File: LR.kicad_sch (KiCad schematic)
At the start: 41 parts, among them J7 Conn_01x01_Pin, J8 Conn_01x01_Pin, J9 Conn_01x01_Pin, Q13 NMOS, Q14 NMOS, Q15 NMOS, Q16 NMOS, Q17 NMOS, Q18 NMOS, U5 OPA2196xDGK, U6 MCT8329A1IREER

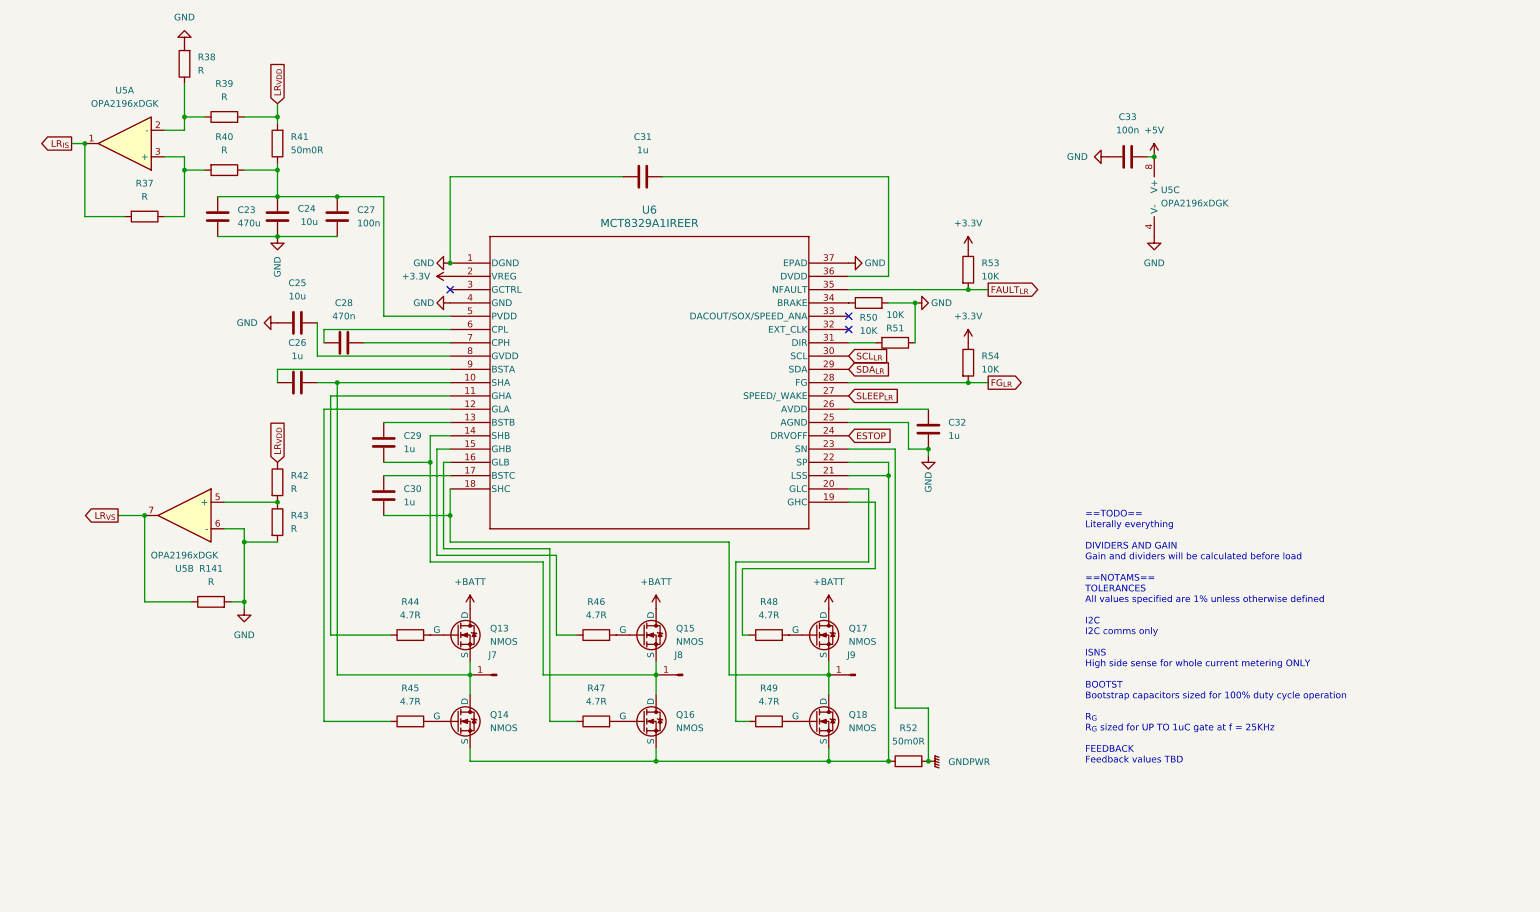
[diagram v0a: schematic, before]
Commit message: The great decluttering
Moved all possible controls to I2C, part selection commenced, IOs assigned pending comms schema
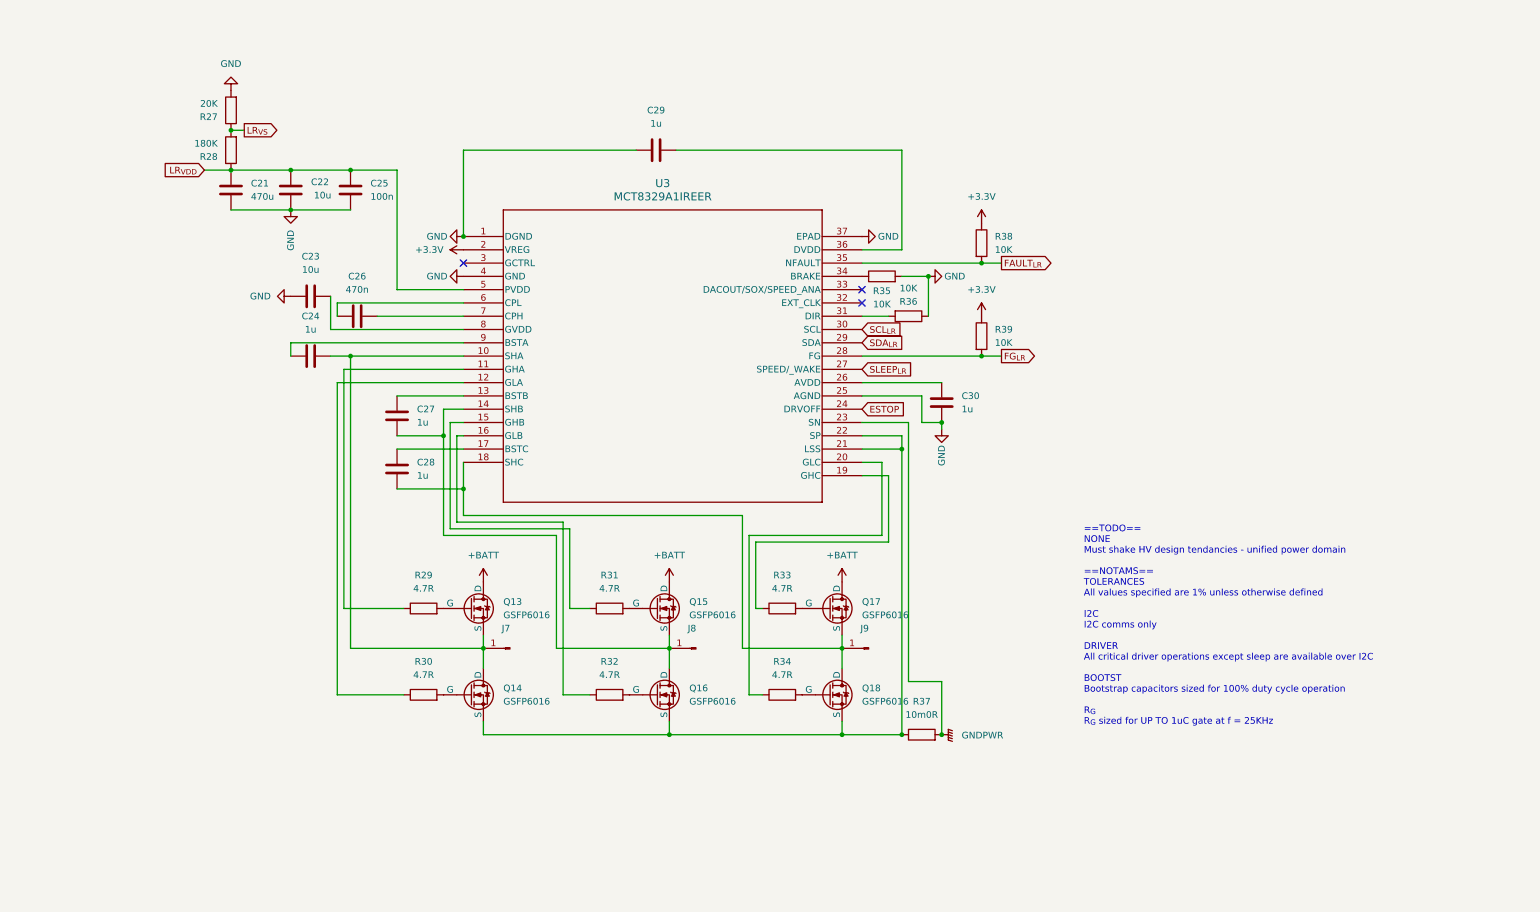
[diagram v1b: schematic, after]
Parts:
- removed C31, C32: 1u, Capacitor_SMD:C_0603_1608Metric, symbol Device:C
- removed C33: 100n, Capacitor_SMD:C_0603_1608Metric, symbol Device:C
- removed R141, R40, R42, R43: R, Resistor_SMD:R_0603_1608Metric_Pad0.98x0.95mm_HandSolder, symbol Device:R
- removed R41, R52: 50m0R, Resistor_SMD:R_1206_3216Metric, symbol Device:R
- removed R44, R45, R46, R47, R48, R49: 4.7R, Resistor_SMD:R_1206_3216Metric, symbol Device:R
- removed R50, R51, R53, R54: 10K, Resistor_SMD:R_0603_1608Metric_Pad0.98x0.95mm_HandSolder, symbol Device:R
- removed U5: OPA2196xDGK, Package_SO:VSSOP-8_3x3mm_P0.65mm, symbol Amplifier_Operational:OPA2196xDGK
- removed U6: MCT8329A1IREER, footprints:WQFN36_REE_TEX, symbol MCT8329:MCT8329A1IREER
- added C21: 470u, Capacitor_SMD:C_0603_1608Metric, symbol Device:C
- added C22: 10u, Capacitor_SMD:C_0603_1608Metric, symbol Device:C
- added R27: 20K, Resistor_SMD:R_0603_1608Metric_Pad0.98x0.95mm_HandSolder, symbol Device:R
- added R28: 180K, Resistor_SMD:R_0603_1608Metric_Pad0.98x0.95mm_HandSolder, symbol Device:R
- added R29, R30, R31, R32, R33, R34: 4.7R, Resistor_SMD:R_1206_3216Metric, symbol Device:R
- added R35, R36: 10K, Resistor_SMD:R_0603_1608Metric_Pad0.98x0.95mm_HandSolder, symbol Device:R
- added U3: MCT8329A1IREER, footprints:WQFN36_REE_TEX, symbol MCT8329:MCT8329A1IREER
- C23: value 470u -> 10u
- C24: value 10u -> 1u
- C25: value 10u -> 100n
- C26: value 1u -> 470n
- C27: value 100n -> 1u
- C28: value 470n -> 1u
- Q13, Q14, Q15, Q16, Q17, Q18: value NMOS -> GSFP6016; footprint (none) -> Package_DFN_QFN:PQFN-8-EP_6x5mm_P1.27mm_Generic
- R37: value R -> 10m0R; footprint Resistor_SMD:R_0603_1608Metric_Pad0.98x0.95mm_HandSolder -> Resistor_SMD:R_1206_3216Metric
- R38, R39: value R -> 10K
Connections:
- net LR_{IS} is gone; now on net GNDPWR: R37.2
- net +3.3V: now also R38.1, R39.1, U3.2 (VREG)
- net ESTOP: now also U3.24 (DRVOFF)
- net FAULT_{LR}: now also R38.2, U3.35 (NFAULT)
- net FG_{LR}: now also R39.2, U3.28 (FG)
- net GND: now also C23.1, C25.2, C29.1, C30.1, C21.2, C22.2, R27.2, R35.2, R36.1, U3.1 (DGND), U3.25 (AGND), U3.37 (EPAD), U3.4 (GND); no longer C23.2, C24.2, C25.1, C27.2, R38.2
- net GNDPWR: now also U3.23 (SN)
- net LR_{VDD}: now also C25.1, C21.1, C22.1, R28.1, U3.5 (PVDD); no longer R39.2
- net LR_{VS}: now also R27.1, R28.2
- net SCL_{LR}: now also U3.30 (SCL)
- net SDA_{LR}: now also U3.29 (SDA)
- net SLEEP_{LR}: now also U3.27 (SPEED/_WAKE)
- net at Q16.2 (G): now also R32.2
- net at J7.1 (Pin_1), Q13.3 (S), Q14.1 (D): now also C24.1, U3.10 (SHA); no longer C26.1
- net at Q14.2 (G): now also R30.2
- net at Q14.3 (S), Q16.3 (S), Q18.3 (S): now also R37.1, U3.21 (LSS), U3.22 (SP)
- net at Q13.2 (G): now also R29.2
- net at J9.1 (Pin_1), Q17.3 (S), Q18.1 (D): now also C28.2, U3.18 (SHC); no longer C30.2
- net at C26.2: now also U3.7 (CPH)
- net at Q18.2 (G): now also R34.2
- net at C28.1: now also U3.17 (BSTC)
- net at J8.1 (Pin_1), Q15.3 (S), Q16.1 (D): now also C27.2, U3.14 (SHB); no longer C29.2
- net at Q17.2 (G): now also R33.2
- net at Q15.2 (G): now also R31.2
- new net: R33.1, U3.19 (GHC)
- new net: C30.2, U3.26 (AVDD)
- new net: C29.2, U3.36 (DVDD)
- new net: C27.1, U3.13 (BSTB)
- new net: R32.1, U3.16 (GLB)
- new net: R29.1, U3.11 (GHA)
- new net: R30.1, U3.12 (GLA)
- new net: R31.1, U3.15 (GHB)
- new net: R34.1, U3.20 (GLC)
- new net: R36.2, U3.31 (DIR)
- new net: R35.1, U3.34 (BRAKE)
- new net: C26.1, U3.6 (CPL)
- new net: C23.2, U3.8 (GVDD)
- new net: C24.2, U3.9 (BSTA)
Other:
- note added: "==TODO== NONE Must shake HV design tendancies - unified power domain ==NOTAMS== TOLERANCES All values specified are 1% unless otherwise defined I2C I2C comms only DRIVER All critical driver operations except sleep are available over I2C BOOTST Bootstrap capacitors sized for 100% duty cycle operation R_{G} R_{G} sized for UP TO 1uC gate at f = 25KHz"
- note removed: "==TODO== Literally everything DIVIDERS AND GAIN Gain and dividers will be calculated before load ==NOTAMS== TOLERANCES All values specified are 1% unless otherwise defined I2C I2C comms only ISNS High side sense for whole current metering ONLY BOOTST Bootstrap capacitors sized for 100% duty cycle operation R_{G} R_{G} sized for UP TO 1uC gate at f = 25KHz FEEDBACK Feedback values TBD"

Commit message: Powerstage
Powerstage layout, non critical changes to schematic
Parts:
- removed C25: 100n, Capacitor_SMD:C_0603_1608Metric, symbol Device:C
- removed J7, J8, J9: Conn_01x01_Pin, symbol Connector:Conn_01x01_Pin
- removed Q13, Q14, Q15, Q16, Q17, Q18: GSFP6016, Package_DFN_QFN:PQFN-8-EP_6x5mm_P1.27mm_Generic, symbol Simulation_SPICE:NMOS
- removed R37: 10m0R, Resistor_SMD:R_1206_3216Metric, symbol Device:R
- added J3: 1724470408, footprints:CONN08_1724470408_MOL, symbol 1724470408:1724470408
- added Q13, Q14, Q15, Q16, Q17, Q18: GSFP6016, Package_SO:PowerPAK_SO-8_Single, symbol Transistor_FET:SiR696DP
- added R37: WSL3637R0100FEA, WSL3637_VIS, symbol WSL3637R0100FEA:WSL3637R0100FEA
- C21: footprint Capacitor_SMD:C_0603_1608Metric -> Capacitor_THT:CP_Radial_D10.0mm_P5.00mm
- C22: footprint Capacitor_SMD:C_0603_1608Metric -> Capacitor_SMD:C_1210_3225Metric
- C23: footprint Capacitor_SMD:C_0603_1608Metric -> Capacitor_SMD:C_0402_1005Metric
- C24, C26, C27, C28, C29, C30: footprint Capacitor_SMD:C_0603_1608Metric -> Capacitor_SMD:C_0201_0603Metric
- R27, R28, R35, R36, R38, R39: footprint Resistor_SMD:R_0603_1608Metric_Pad0.98x0.95mm_HandSolder -> Resistor_SMD:R_0201_0603Metric
- R29, R30, R31, R32, R33, R34: value 4.7R -> 4R7; footprint Resistor_SMD:R_1206_3216Metric -> Resistor_SMD:R_0603_1608Metric
- U3: footprint footprints:WQFN36_REE_TEX -> WQFN36_REE_TEX
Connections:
- net GNDPWR: now also J3.4, J3.8, R37.4; no longer U3.23 (SN)
- net LR_{VDD}: now also Q13.5 (D), Q15.5 (D), Q17.5 (D)
- net at R29.2: now also Q13.4 (G)
- net at C24.1, U3.10 (SHA): now also J3.1, J3.5, Q13.1 (S), Q13.2 (S), Q13.3 (S), Q14.5 (D)
- net at C28.2, U3.18 (SHC): now also J3.3, J3.7, Q17.1 (S), Q17.2 (S), Q17.3 (S), Q18.5 (D)
- net at R34.2: now also Q18.4 (G)
- net at U3.21 (LSS), U3.22 (SP): now also R37.2
- net at R33.2: now also Q17.4 (G)
- net at R31.2: now also Q15.4 (G)
- net at C27.2, U3.14 (SHB): now also J3.2, J3.6, Q15.1 (S), Q15.2 (S), Q15.3 (S), Q16.5 (D)
- net at R32.2: now also Q16.4 (G)
- net at U3.6 (CPL): now also C26.2; no longer C26.1
- net at U3.7 (CPH): now also C26.1; no longer C26.2
- net at R30.2: now also Q14.4 (G)
- new net: Q14.1 (S), Q14.2 (S), Q14.3 (S), Q16.1 (S), Q16.2 (S), Q16.3 (S), Q18.1 (S), Q18.2 (S), Q18.3 (S), R37.1
- new net: R37.3, U3.23 (SN)
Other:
- note added: "==TODO== NONE Must shake HV design tendancies - unified power domain ==NOTAMS== TOLERANCES All values specified are 1% unless otherwise defined I2C I2C comms only DRIVER All critical driver operations except sleep are available over I2C BOOTST Bootstrap capacitors sized for 100% duty cycle operation R_{G} R_{G} sized for UP TO 1uC gate at f = 25KHz SUBSTRATE TEMP PCB will not comply with IEC boar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"
- note removed: "==TODO== NONE Must shake HV design tendancies - unified power domain ==NOTAMS== TOLERANCES All values specified are 1% unless otherwise defined I2C I2C comms only DRIVER All critical driver operations except sleep are available over I2C BOOTST Bootstrap capacitors sized for 100% duty cycle operation R_{G} R_{G} sized for UP TO 1uC gate at f = 25KHz"
